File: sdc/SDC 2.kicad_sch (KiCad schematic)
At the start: 82 parts, among them J1 Conn_02x10_Odd_Even, K1 G2RL-2A, K2 G2RL-2A, K3 G2RL-2A, K4 G2RL-2A, Q1 2N7002, Q2 2N7002, Q3 2N7002, Q4 2N7002, Q5 2N7002, Q6 2N7002, U1 VOM618AT, U10 AP2204K-ADJ, U2 VOM618AT, U3 AS331KTR-G1, U4 AS331KTR-G1, U5 AS331KTR-G1, U6 VOM618AT, U7 VOM618AT, U9 AP2204K-ADJ

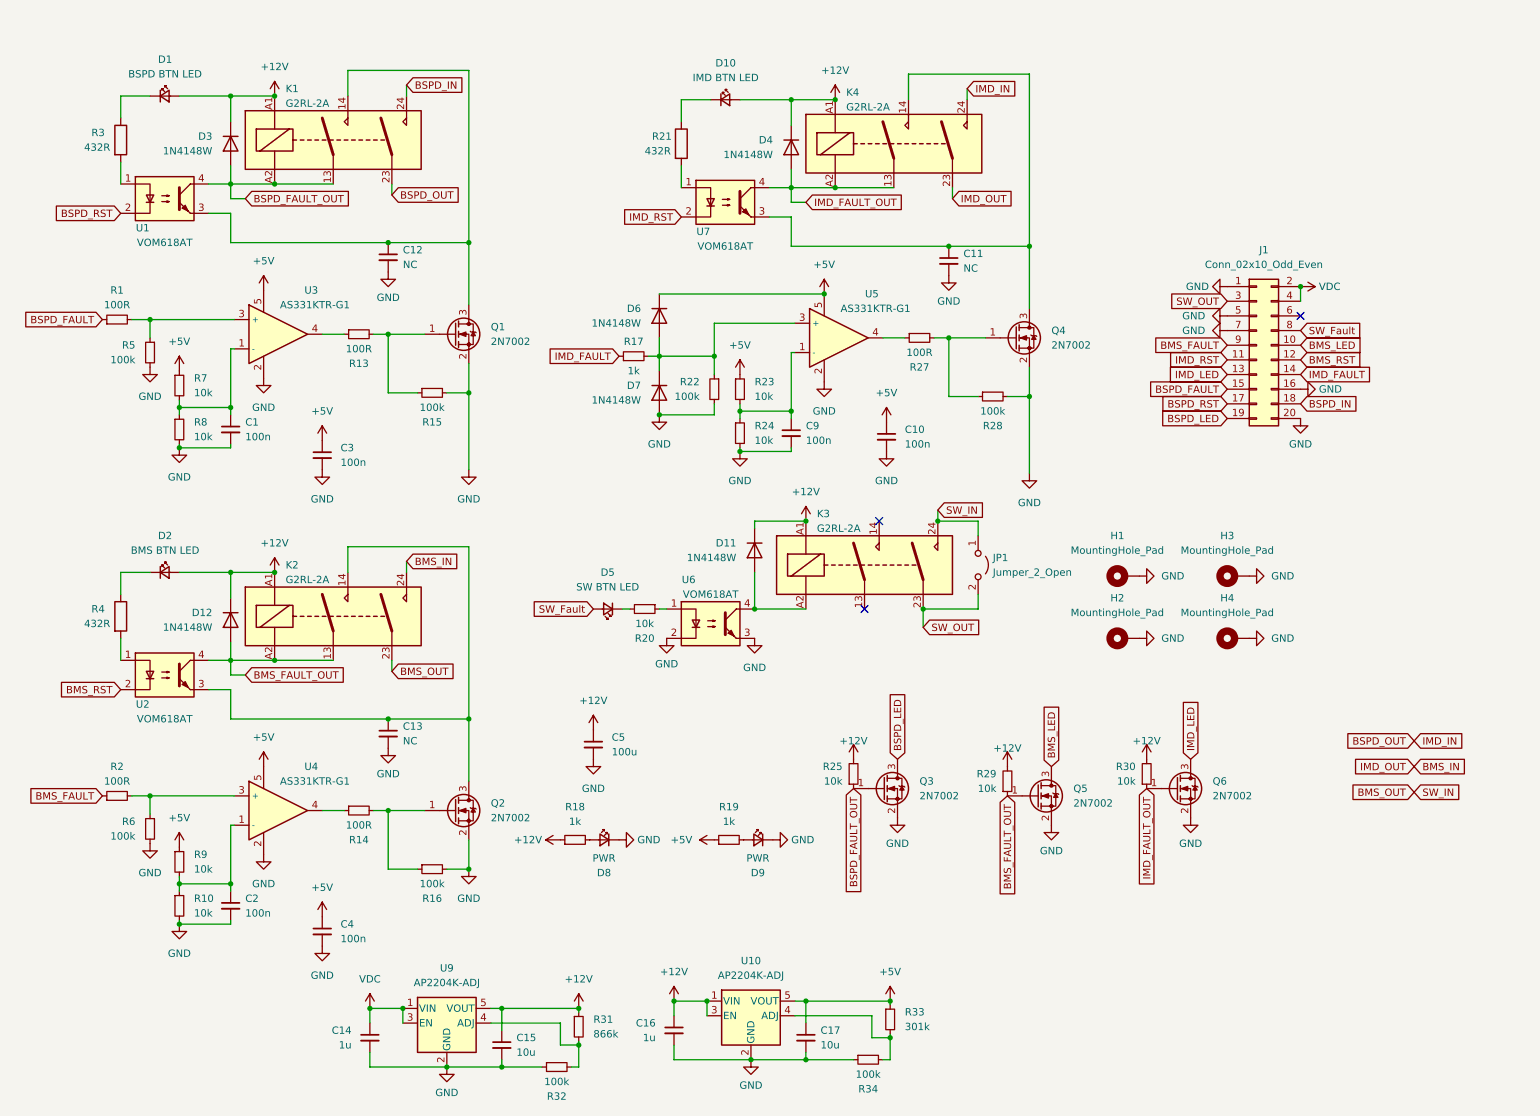
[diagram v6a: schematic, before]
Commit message: add pull up Resistor
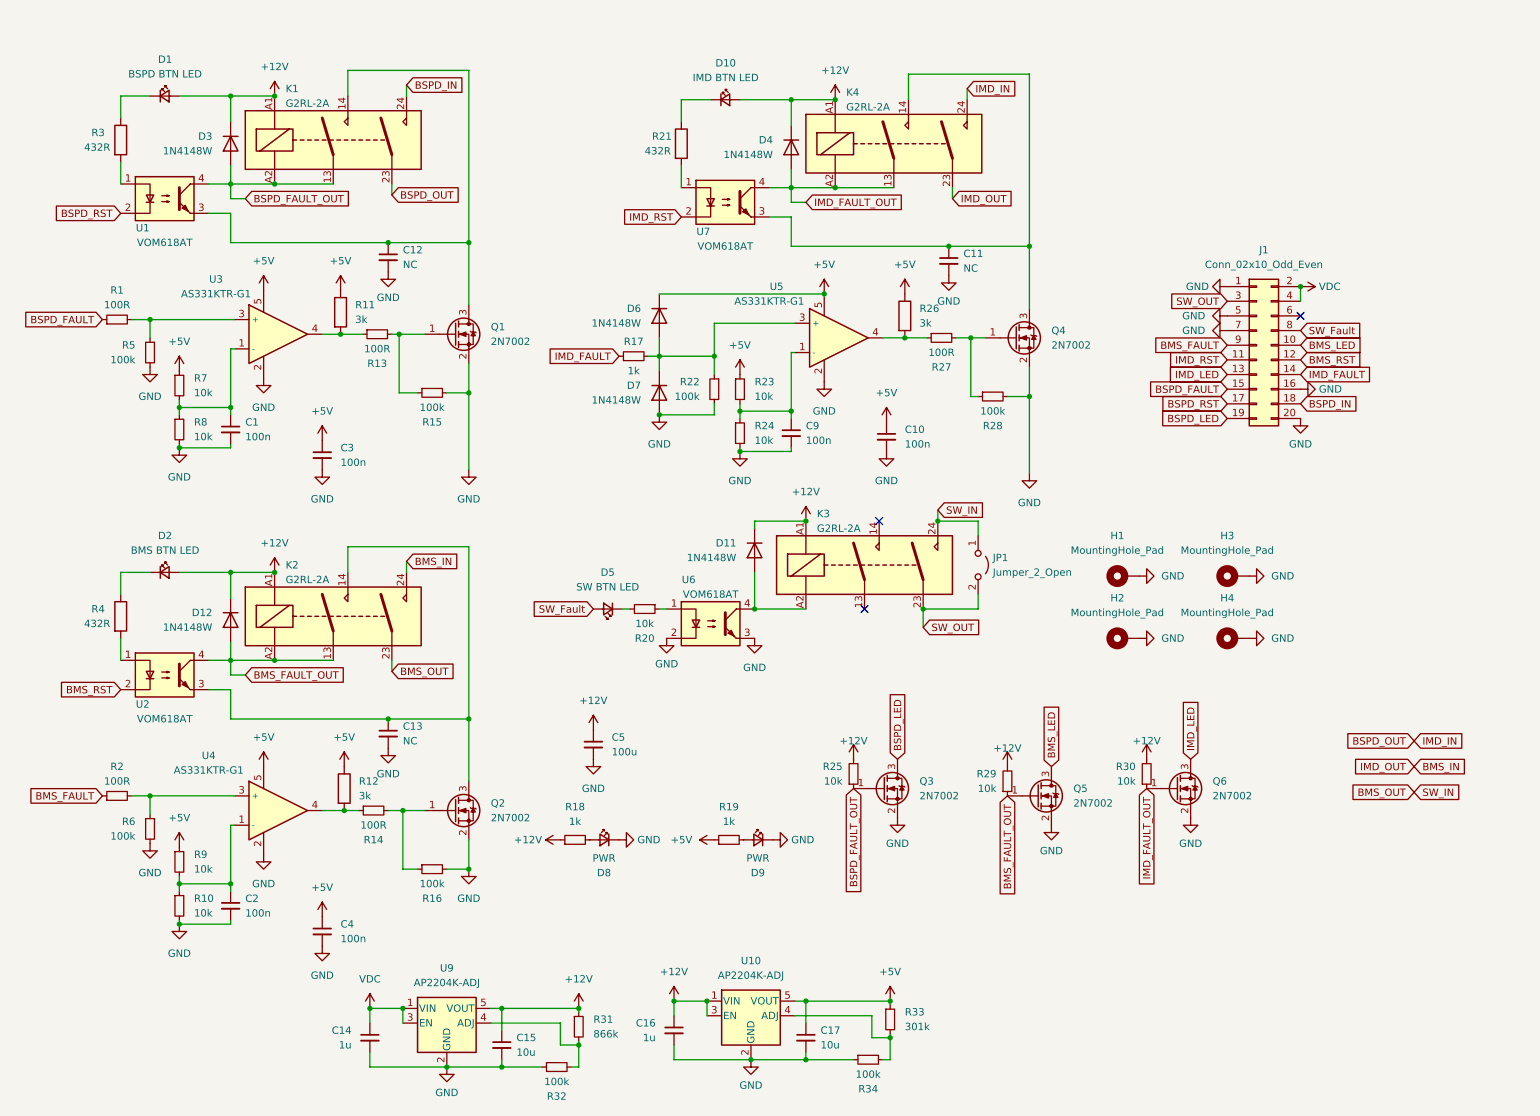
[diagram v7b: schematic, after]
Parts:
- added R11, R12, R26: 3k, Resistor_SMD:R_0603_1608Metric, symbol Device:R
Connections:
- net +5V: now also R11.1, R12.1, R26.1
- net at R27.1, U5.4: now also R26.2
- net at R14.1, U4.4: now also R12.2
- net at R13.1, U3.4: now also R11.2
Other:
- moved on the sheet: R13, R14, R27
